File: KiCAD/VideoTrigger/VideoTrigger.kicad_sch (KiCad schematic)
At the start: 14 parts

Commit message: Updated README and schematic
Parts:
- removed A?: Arduino_UNO_R2, Module:Arduino_UNO_R2, symbol MCU_Module:Arduino_UNO_R2
- removed D? (x2): D, symbol Device:D
- removed Q?: Q_NPN_BCE, symbol Device:Q_NPN_BCE
- removed R? (x2): R, symbol Device:R
- removed U? (x2): 74LS109, symbol 74xx:74LS109
- removed U?: EA_T123X-I2C, Display:EA_T123X-I2C, symbol Display_Character:EA_T123X-I2C
- added C1: C, symbol Device:C
- added C2: 510p, symbol Device:C
- added C3, C4, C7, C8: 100n, symbol Device:C
- added C5, C6: 22p, symbol Device:C
- added D1: LED, symbol Device:LED
- added D2, D3, D4: 1N914, symbol Device:D
- added J1: Video In, symbol Connector:Conn_Coaxial
- added J2: ICSP, symbol Connector_Generic:Conn_02x03_Odd_Even
- added J3: Conn_01x02, symbol Connector_Generic:Conn_01x02
- added J4: Conn_01x04, symbol Connector_Generic:Conn_01x04
- added J5: Trigger Out, symbol Connector:Conn_Coaxial
- added Q1: 2N3904, symbol Device:Q_NPN_BCE
- added R1: 620R, symbol Device:R
- added R2: 680K, symbol Device:R
- added R3, R5: 1K, symbol Device:R
- added R4, R6: 10K, symbol Device:R
- added SW1: RESET, symbol Switch:SW_Push
- added unit 2 of U3
- added unit 1 of U3
- added U4: DISPLAY_SSD1306_OLED_128x32, symbol UKMaker:DISPLAY_SSD1306_OLED_128x32
- added Y1: 20MHz, symbol Device:Crystal_Small
- R7: renamed from R?; value R -> 10K
- gave numbers to parts that had none: 4
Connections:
- net +5V: now also U1.20 (AVCC), U1.7 (VCC), U2.8 (VCC), U3.16 (VCC), C1.1, C8.1, D2.1 (K), J2.2 (Pin_2), J3.2 (Pin_2), J4.3 (Pin_3), R4.1, R5.1, U3.11 (~{S}), U3.13 (~{K}), U3.14 (J), U3.2 (J), U3.3 (~{K}), U3.5 (~{S}), U4.2 (VCC)
- net ARM: now also U1.13 (PD7), U3.1 (~{R})
- net ARMN: now also U1.12 (PD6), U3.15 (~{R})
- net ENCA: now also U1.18 (PB4), J2.1 (Pin_1)
- net ENCB: now also U1.17 (PB3), J2.4 (Pin_4)
- net GND: now also U1.22 (GND), U1.8 (GND), U2.4 (GND), U3.8 (GND), C1.2, C2.2, C4.2, C5.1, C6.1, C7.2, C8.2, J1.2 (Ext), J2.6 (Pin_6), J3.1 (Pin_1), J4.4 (Pin_4), J5.2 (Ext), Q1.3 (E), R2.1, R3.2, SW1.2, U4.1 (GND)
- net SW: now also U1.16 (PB2)
- net CSYNC: now reaches U2.1 (CSYNC)
- net CSYNC: now also U1.4 (PD2), R6.2, U3.4 (C)
- net FRAME: now reaches U2.3 (FRAME)
- net FRAME: now also U1.5 (PD3)
- net at U2.2 (VIDEO): now also C3.1
- net at U2.6 (INT): now also C4.1, R2.2
- net at U1.1 (~{RESET}/PC6): now also C7.1, D2.2 (A), J2.5 (Pin_5), R4.2, SW1.1
- net at U1.10 (XTAL2/PB7): now also C6.2, Y1.1
- net at U1.19 (PB5): now also D1.2 (A), J2.3 (Pin_3)
- net SDA: now reaches U1.27 (PC4)
- net SDA: now also J4.1 (Pin_1), U4.4 (SDA)
- net SCL: now reaches U1.28 (PC5)
- net SCL: now also J4.2 (Pin_2), U4.3 (SCL)
- net at U1.9 (XTAL1/PB6): now also C5.2, Y1.2
- net TRIGGERN: no longer names the net of R7.2
- net TRIGGERN: now also D3.2 (A), D4.2 (A), J5.1 (In)
- new net: Q1.2 (C), R5.2, U3.12 (C)
- new net: D3.1 (K), U3.9 (~{Q})
- new net: Q1.1 (B), R6.1
- new net: C2.1, C3.2, R1.2
- new net: D4.1 (K), U3.7 (~{Q})
- new net: D1.1 (K), R3.1
- new net: J1.1 (In), R1.1
- no-connect marks 0 -> 15
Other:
- company: (none) -> Duncan McIntyre (UKMaker)
- title: (none) -> Video Trigger
- moved on the sheet: R7, SW2, U1, U2, U3C

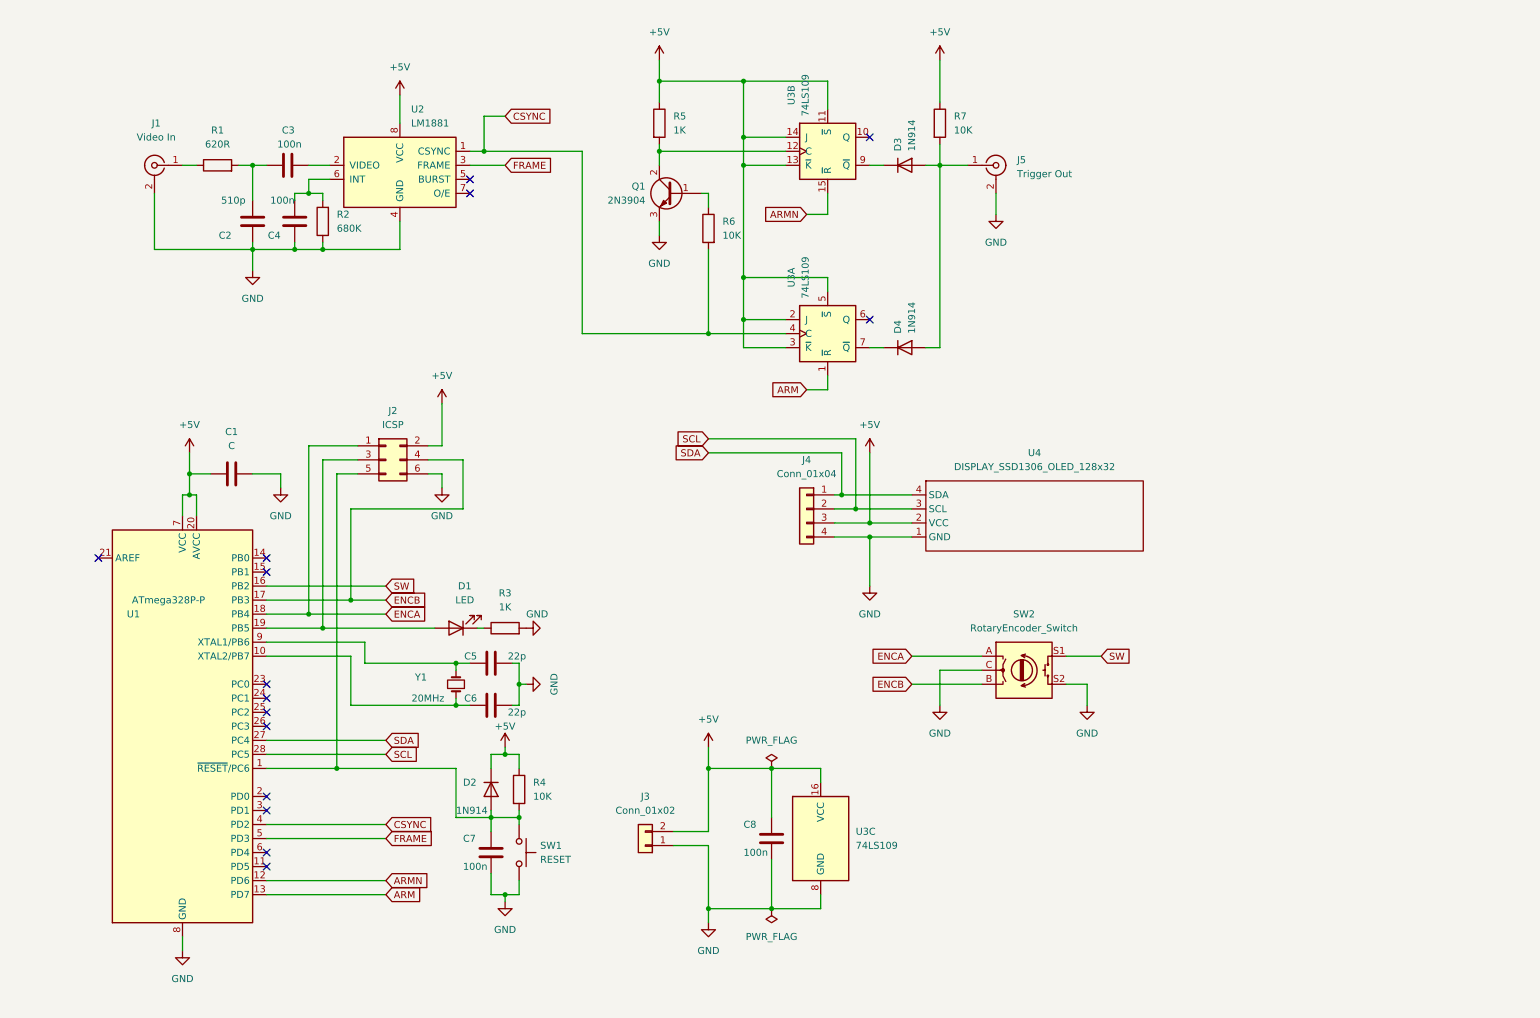
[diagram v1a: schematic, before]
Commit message: Added input buffering, updated README
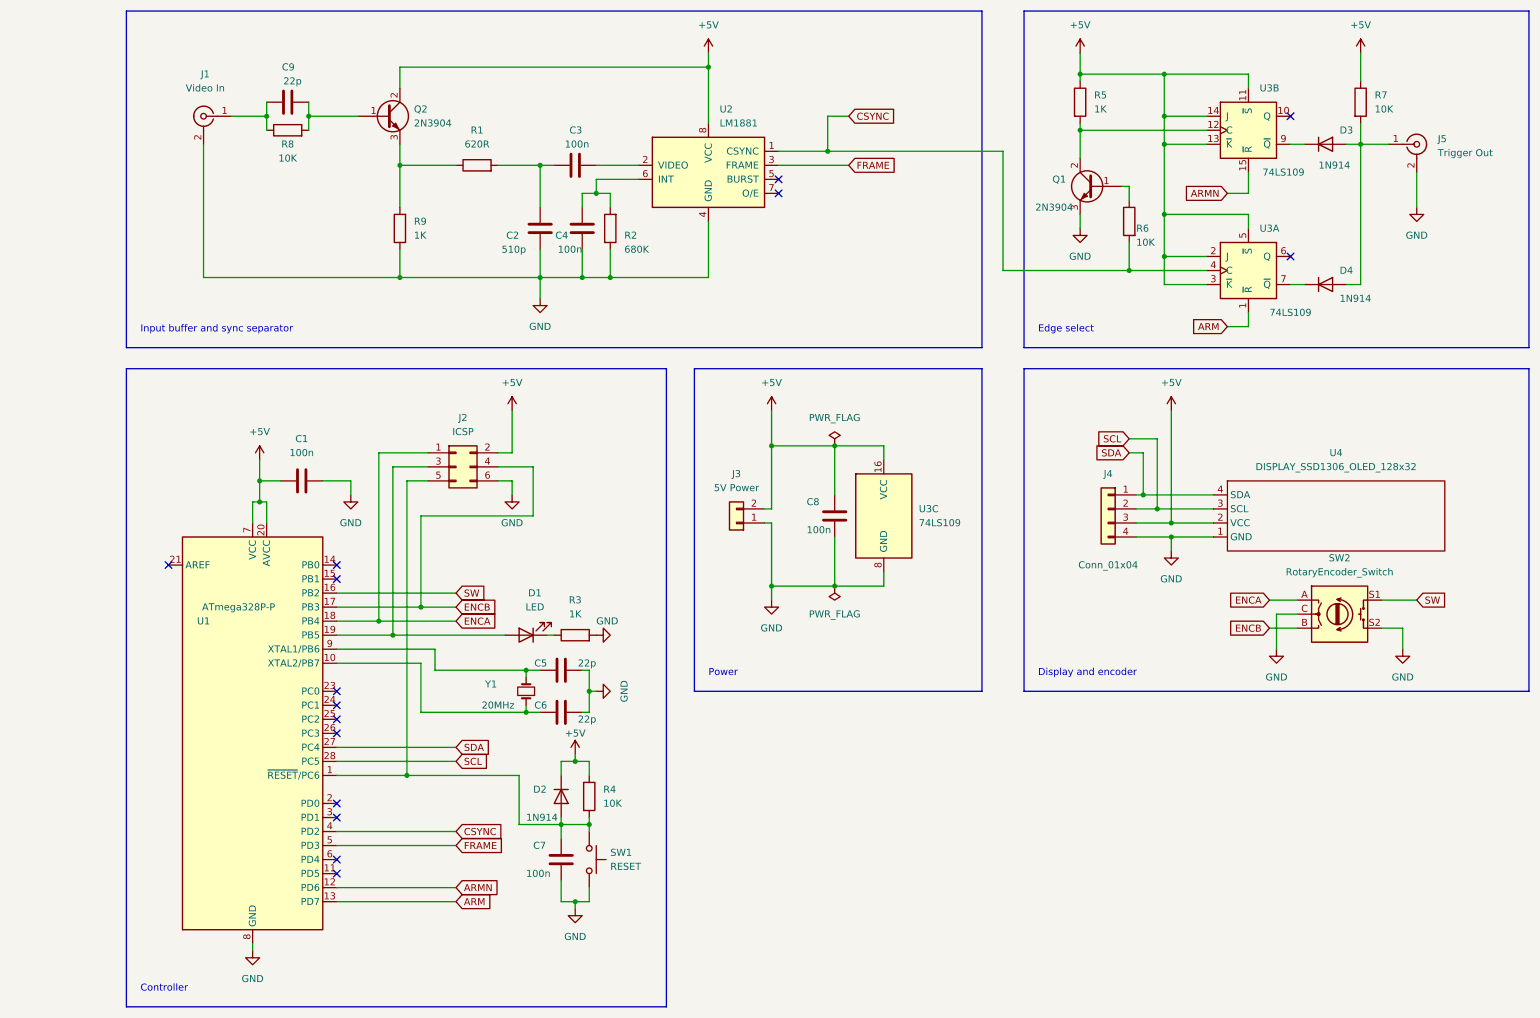
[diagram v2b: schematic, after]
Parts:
- added C9: 22p, symbol Device:C
- added Q2: 2N3904, symbol Device:Q_NPN_BCE
- added R8: 10K, symbol Device:R
- added R9: 1K, symbol Device:R
- C1: value C -> 100n
- J3: value Conn_01x02 -> 5V Power
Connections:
- net +5V: now also Q2.2 (C)
- net GND: now also R9.1
- net at J1.1 (In): now also C9.2, R8.1; no longer R1.1
- new net: C9.1, Q2.1 (B), R8.2
- new net: Q2.3 (E), R1.1, R9.2
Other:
- note added: "Controller"
- note added: "Display and encoder"
- note added: "Edge select"
- note added: "Input buffer and sync separator"
- note added: "Power"
- moved on the sheet: C1, C2, C3, C4, C5, C6, C7, C8, D1, D2, D3, D4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

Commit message: Added PCB layout. Some signal changes to make routing easier
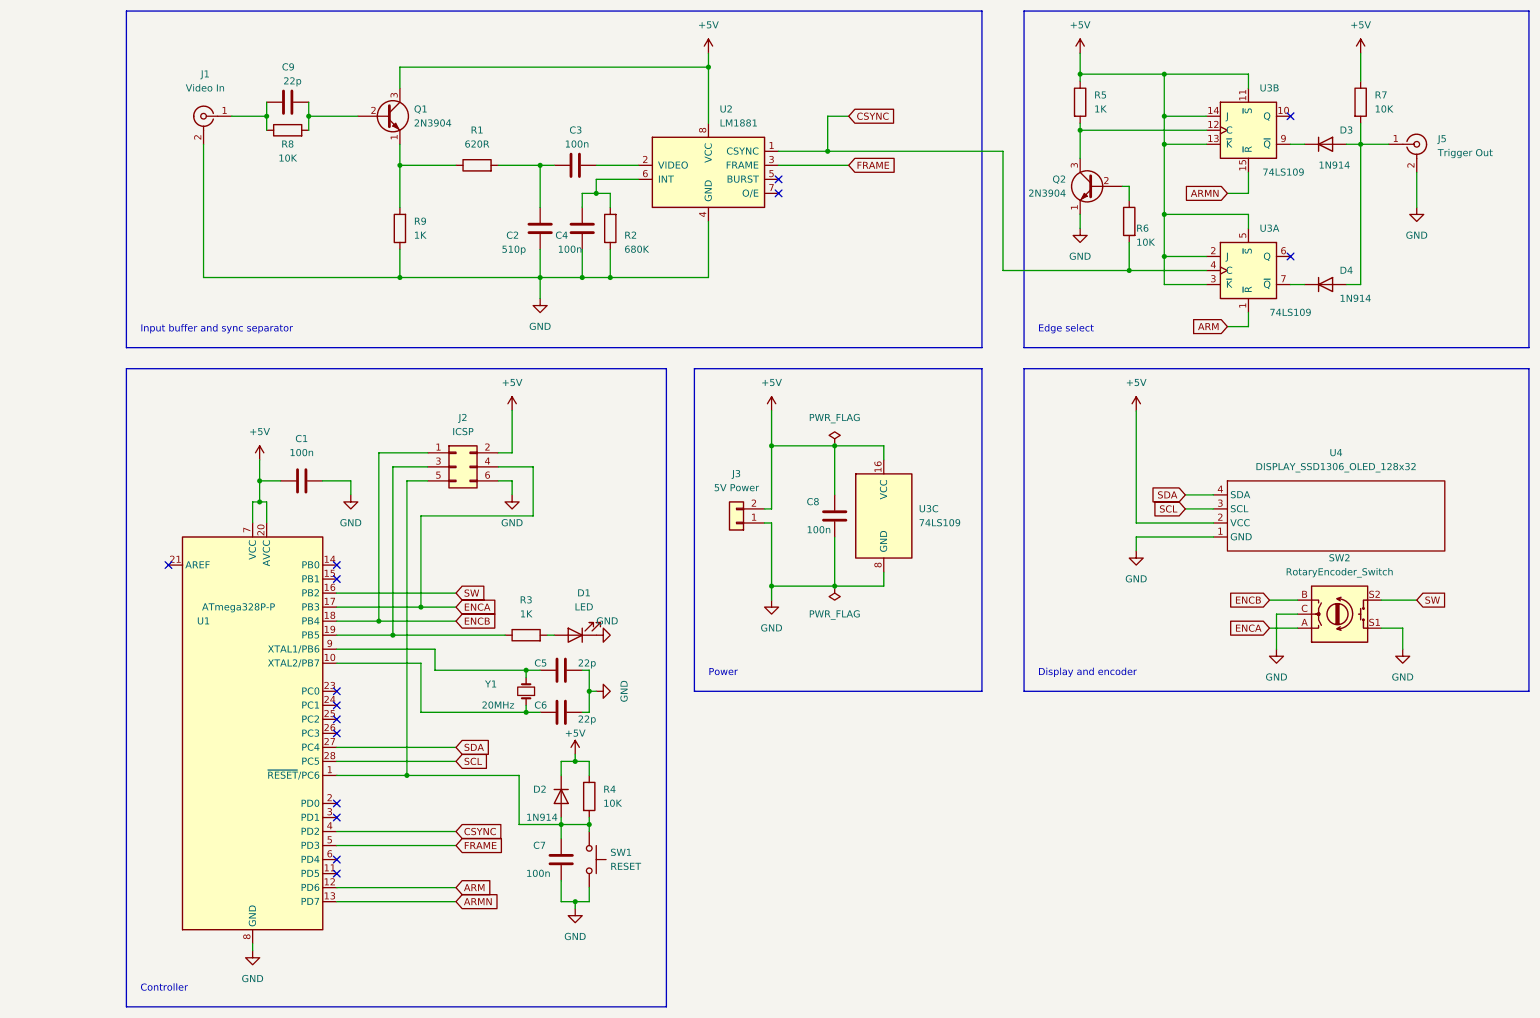
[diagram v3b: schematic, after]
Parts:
- removed J4: Conn_01x04, symbol Connector_Generic:Conn_01x04
- removed Q1, Q2: 2N3904, symbol Device:Q_NPN_BCE
- added Q1, Q2: 2N3904, Package_TO_SOT_THT:TO-92L_Inline_Wide, symbol Device:Q_NPN_EBC
- C1, C2, C3, C4, C5, C6, C7, C8, C9: footprint (none) -> Capacitor_THT:C_Disc_D4.3mm_W1.9mm_P5.00mm
- D1: footprint (none) -> LED_THT:LED_D3.0mm
- D2, D3, D4: footprint (none) -> Diode_THT:D_DO-34_SOD68_P7.62mm_Horizontal
- J1, J5: footprint (none) -> Connector_Coaxial:SMA_Amphenol_901-144_Vertical
- J2: footprint (none) -> Connector_PinHeader_2.54mm:PinHeader_2x03_P2.54mm_Vertical
- J3: footprint (none) -> TerminalBlock:TerminalBlock_bornier-2_P5.08mm
- R1, R2, R3, R4, R5, R6, R7, R8, R9: footprint (none) -> Resistor_THT:R_Axial_DIN0207_L6.3mm_D2.5mm_P7.62mm_Horizontal
- SW1: footprint (none) -> Button_Switch_THT:SW_TH_Tactile_Omron_B3F-10xx
- SW2: footprint (none) -> Rotary_Encoder:RotaryEncoder_Alps_EC11E-Switch_Vertical_H20mm
- U2: footprint (none) -> Package_DIP:DIP-8_W7.62mm_LongPads
- U3: footprint (none) -> Package_DIP:DIP-16_W7.62mm_LongPads
- U4: footprint (none) -> Connector_PinHeader_2.54mm:PinHeader_1x04_P2.54mm_Vertical
- Y1: footprint (none) -> Crystal:Crystal_HC49-U_Vertical
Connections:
- net +5V: now also Q1.3 (C)
- net ARM: now also U1.12 (PD6); no longer U1.13 (PD7)
- net ARMN: now also U1.13 (PD7); no longer U1.12 (PD6)
- net ENCA: now also J2.4 (Pin_4), U1.17 (PB3); no longer J2.1 (Pin_1), U1.18 (PB4)
- net ENCB: now also J2.1 (Pin_1), U1.18 (PB4); no longer J2.4 (Pin_4), U1.17 (PB3)
- net GND: now also D1.1 (K), SW2.S1, Q2.1 (E); no longer R3.2, SW2.S2
- net SW: now also SW2.S2; no longer SW2.S1
- net at R5.2, U3.12 (C): now also Q2.3 (C)
- net at R6.1: now also Q2.2 (B)
- net at C9.1, R8.2: now also Q1.2 (B)
- net at J2.3 (Pin_3), U1.19 (PB5): now also R3.1; no longer D1.2 (A)
- net at R1.1, R9.2: now also Q1.1 (E)
- new net: D1.2 (A), R3.2
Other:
- moved on the sheet: D1, R3
